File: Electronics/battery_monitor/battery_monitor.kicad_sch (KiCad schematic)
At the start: 23 parts, among them IC1 MIC2779H-1YM5_TR, J2 Conn_01x02_Pin, J2 Conn_01x04_Male, J3 Conn_01x02_Pin, Q2 DMP4015SK3-13, Q4 BSS123LT1G, U1 MCP1700x-120xxMB, U2 INA226

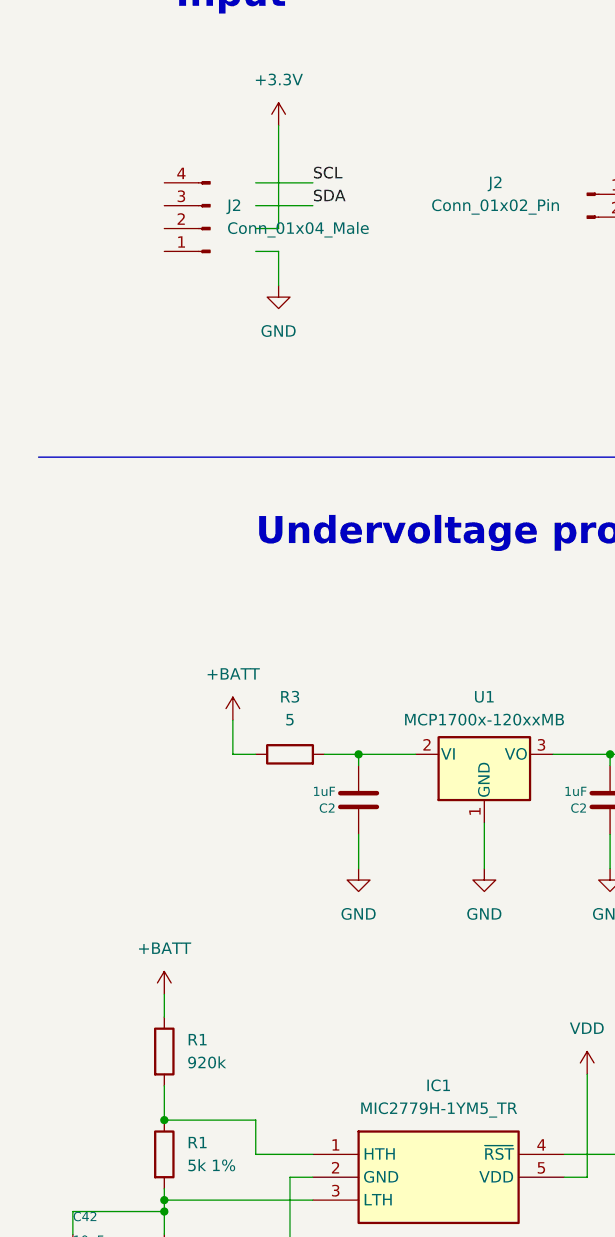
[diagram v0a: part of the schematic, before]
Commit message: Add main robot PCB
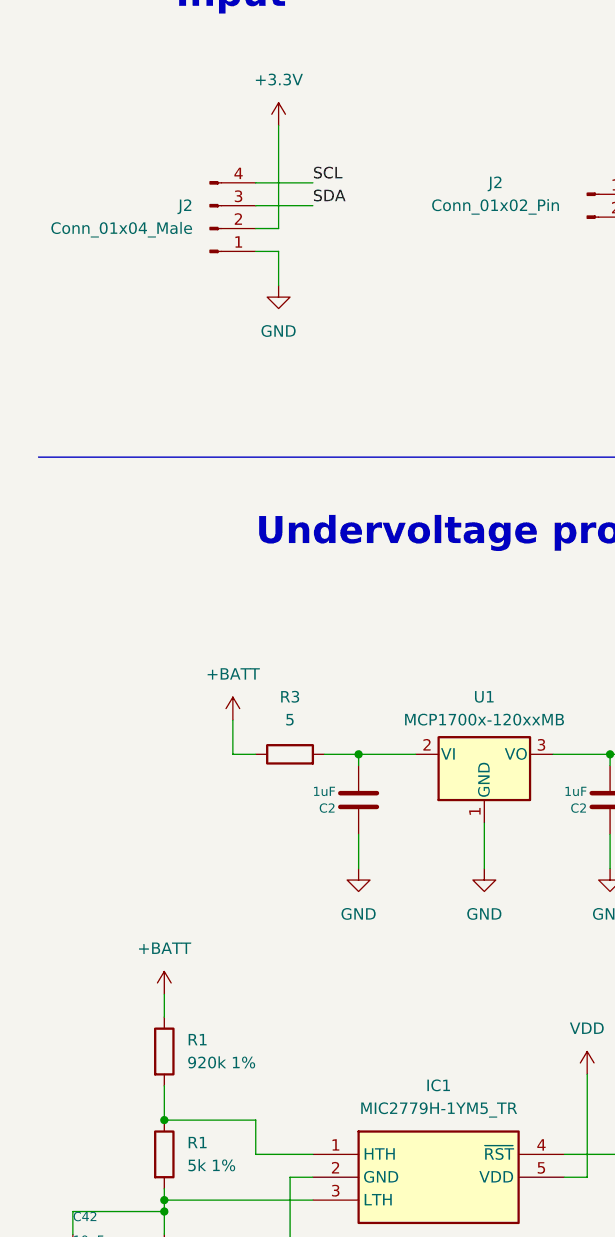
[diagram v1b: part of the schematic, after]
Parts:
- C2: RS (none) -> 103-4095
- JP1, JP2: now left out of the parts list
- R1: Mouser (none) -> 71-CRCW0805-5K
- R1: value 920k -> 920k 1%; Mouser (none) -> 660-RN73H2ATD9203B25
- R1: Mouser (none) -> 603-RC0805FR-0775KL
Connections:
- net +3.3V: now also J2.2 (Pin_2)
- net GND: now also J2.1 (Pin_1)
- net SCL: now also J2.4 (Pin_4)
- net SDA: now also J2.3 (Pin_3)
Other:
- moved on the sheet: J2
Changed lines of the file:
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@@
+      (effects (font (size 1.27 1.27)) hide)
+    )
+    (property "Mouser" " 71-CRCW0805-5K " (at 29.21 149.86 0)
       (effects (font (size 1.27 1.27)) hide)
     )
@@
   (symbol (lib_id "Device:R") (at 29.21 138.43 0) (unit 1)
     (in_bom yes) (on_board yes) (dnp no) (fields_autoplaced)
-    (property "Reference" "R1" (at 31.75 137.1599 0)
-      (effects (font (size 1.27 1.27)) (justify left))
-    )
-    (property "Value" "920k" (at 31.75 139.6999 0)
+    (property "Reference" "R1" (at 31.75 137.16 0)
+      (effects (font (size 1.27 1.27)) (justify left))
+    )
+    (property "Value" "920k 1%" (at 31.75 139.7 0)
       (effects (font (size 1.27 1.27)) (justify left))
     )
@@
     )
     (property "RS" "" (at 29.21 138.43 0)
+      (effects (font (size 1.27 1.27)) hide)
+    )
+    (property "Mouser" " 660-RN73H2ATD9203B25 " (at 29.21 138.43 0)
+      (effects (font (size 1.27 1.27)) hide)
+    )
+    (property "Field6" "" (at 29.21 138.43 0)
       (effects (font (size 1.27 1.27)) hide)
     )
@@
   )
   (symbol (lib_id "Jumper:SolderJumper_3_Open") (at 245.11 53.34 90) (mirror x) (unit 1)
-    (in_bom yes) (on_board yes) (dnp no) (fields_autoplaced)
+    (in_bom no) (on_board yes) (dnp no) (fields_autoplaced)
     (property "Reference" "JP1" (at 242.57 52.07 90)
       (effects (font (size 1.27 1.27)) (justify left))
@@
       (effects (font (size 1.27 1.27)) (justify left bottom) hide)
     )
+    (property "RS" "    103-4095" (at 78.74 110.49 0)
+      (effects (font (size 1.27 1.27)) hide)
+    )
     (pin "1")
     (pin "2")
@@
       (effects (font (size 1.27 1.27)) hide)
     )
-    (property "RS" "" (at 29.21 162.56 0)
+    (property "Mouser" " 603-RC0805FR-0775KL " (at 29.21 162.56 0)
+      (effects (font (size 1.27 1.27)) hide)
+    )
+    (property "Field6" "" (at 29.21 162.56 0)
       (effects (font (size 1.27 1.27)) hide)
     )
@@
     )
   )
-  (symbol (lib_id "Connector:Conn_01x04_Male") (at 34.29 46.99 180) (unit 1)
+  (symbol (lib_id "Connector:Conn_01x04_Male") (at 34.29 46.99 0) (mirror x) (unit 1)
     (in_bom yes) (on_board yes) (dnp no)
-    (property "Reference" "J2" (at 36.195 44.4499 0)
+    (property "Reference" "J2" (at 32.385 44.4499 0)
       (effects (font (size 1.27 1.27)) (justify right))
     )
-    (property "Value" "Conn_01x04_Male" (at 36.195 46.9899 0)
+    (property "Value" "Conn_01x04_Male" (at 32.385 46.9899 0)
       (effects (font (size 1.27 1.27)) (justify right))
     )
@@
   )
   (symbol (lib_id "Jumper:SolderJumper_3_Open") (at 266.7 53.34 270) (unit 1)
-    (in_bom yes) (on_board yes) (dnp no) (fields_autoplaced)
+    (in_bom no) (on_board yes) (dnp no) (fields_autoplaced)
     (property "Reference" "JP2" (at 269.24 52.07 90)
       (effects (font (size 1.27 1.27)) (justify left))
@@
       (effects (font (size 1.27 1.27)) (justify left bottom) hide)
     )
-    (pin "1")
+    (property "RS" "    103-4095" (at 50.8 110.49 0)
+      (effects (font (size 1.27 1.27)) hide)
+    )
+    (pin "1")

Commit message: Main robot PCB order
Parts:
- Q4: value BSS123LT1G -> BS170; RS 545-0135 -> 739-0357
- R1: Mouser 71-CRCW0805-5K -> (none); Mouser Part Number (none) -> 71-CRCW0805-5K
- R1: Mouser 660-RN73H2ATD9203B25 -> (none); Mouser Part Number (none) -> 660-RN73H2ATD9203B25
- R1: Mouser 603-RC0805FR-0775KL -> (none); Mouser Part Number (none) -> 603-RC0805FR-0775KL
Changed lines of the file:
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@@
       (effects (font (size 1.27 1.27)) hide)
     )
-    (property "Mouser" " 71-CRCW0805-5K " (at 29.21 149.86 0)
+    (property "Mouser Part Number" " 71-CRCW0805-5K " (at 29.21 149.86 0)
       (effects (font (size 1.27 1.27)) hide)
     )
@@
       (effects (font (size 1.27 1.27)) hide)
     )
-    (property "Mouser" " 660-RN73H2ATD9203B25 " (at 29.21 138.43 0)
+    (property "Mouser Part Number" " 660-RN73H2ATD9203B25 " (at 29.21 138.43 0)
       (effects (font (size 1.27 1.27)) hide)
     )
@@
       (effects (font (size 1.27 1.27)) (justify left))
     )
-    (property "Value" "BSS123LT1G" (at 92.71 151.13 0)
+    (property "Value" "BS170" (at 92.71 151.13 0)
       (effects (font (size 1.27 1.27)) (justify left))
     )
@@
       (effects (font (size 1.27 1.27)) hide)
     )
-    (property "RS" "    545-0135" (at 86.36 149.86 0)
+    (property "RS" "    739-0357" (at 86.36 149.86 0)
       (effects (font (size 1.27 1.27)) hide)
     )
@@
       (effects (font (size 1.27 1.27)) hide)
     )
-    (property "Mouser" " 603-RC0805FR-0775KL " (at 29.21 162.56 0)
-      (effects (font (size 1.27 1.27)) hide)
-    )
+    (property "Mouser Part Number" " 603-RC0805FR-0775KL " (at 29.21 162.56 0)
+      (effects (font (size 1.27 1.27)) hide)
+    )

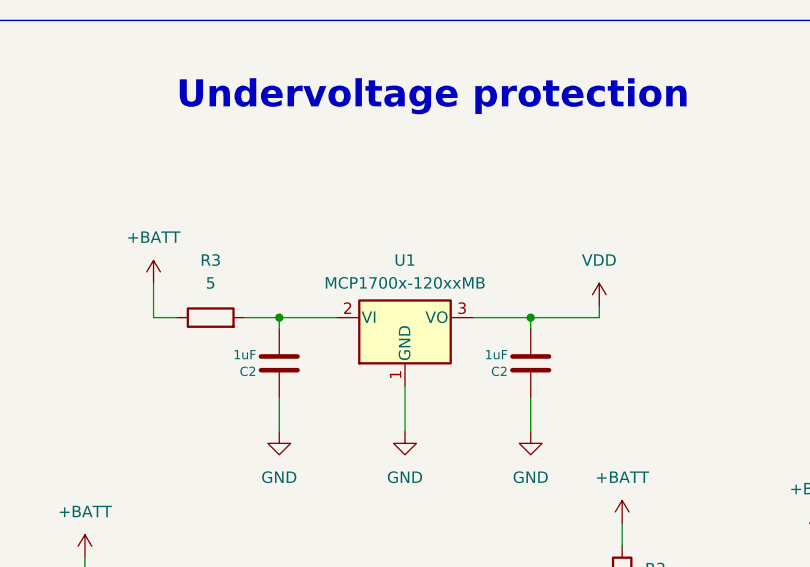
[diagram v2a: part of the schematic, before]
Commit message: Implement fully action-based strategy framework for 2024 robot.
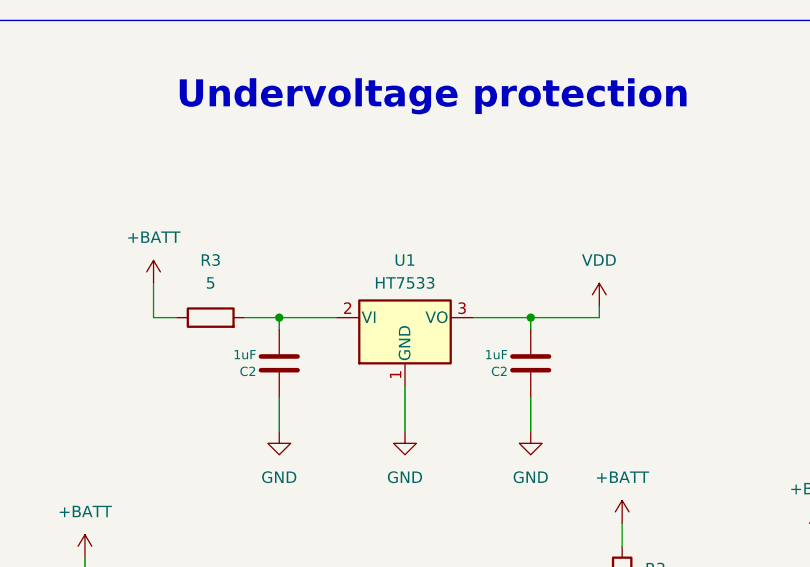
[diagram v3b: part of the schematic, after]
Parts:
- U1: value MCP1700x-120xxMB -> HT7533; RS 669-4923 -> 885-0721
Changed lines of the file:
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@@
       (effects (font (size 1.27 1.27)))
     )
-    (property "Value" "MCP1700x-120xxMB" (at 64.77 101.6 0)
+    (property "Value" "HT7533" (at 64.77 101.6 0)
       (effects (font (size 1.27 1.27)))
     )
@@
       (effects (font (size 1.27 1.27)) hide)
     )
-    (property "RS" "    669-4923" (at 64.77 105.41 0)
+    (property "RS" "    885-0721" (at 64.77 105.41 0)
       (effects (font (size 1.27 1.27)) hide)
     )

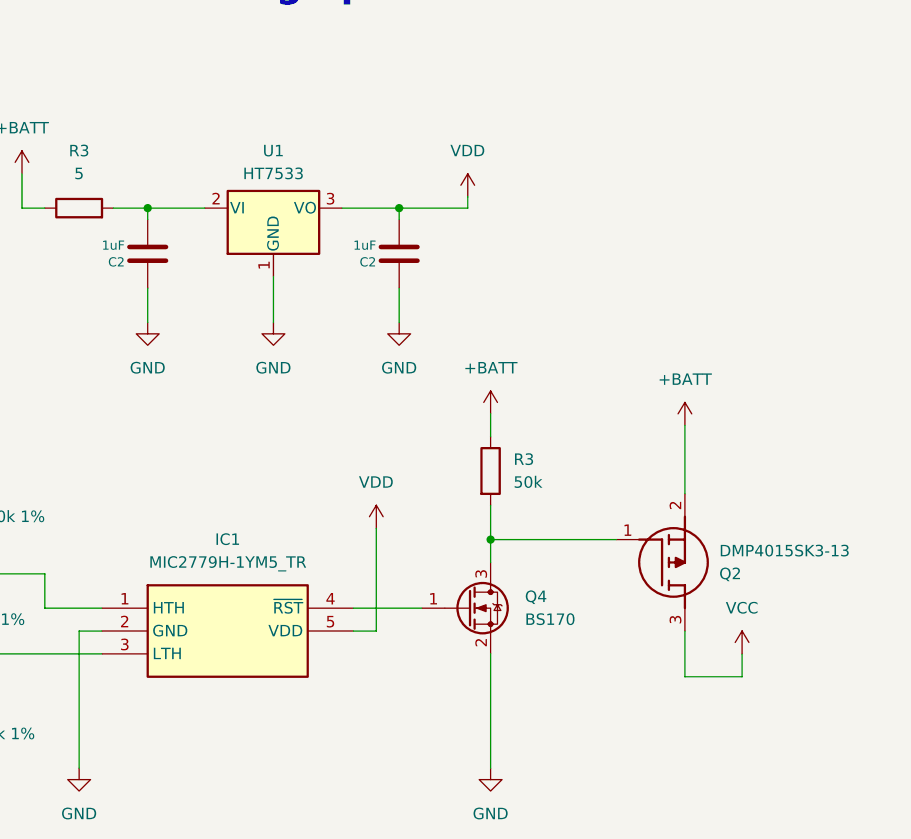
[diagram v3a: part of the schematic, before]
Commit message: Add missing GameState file
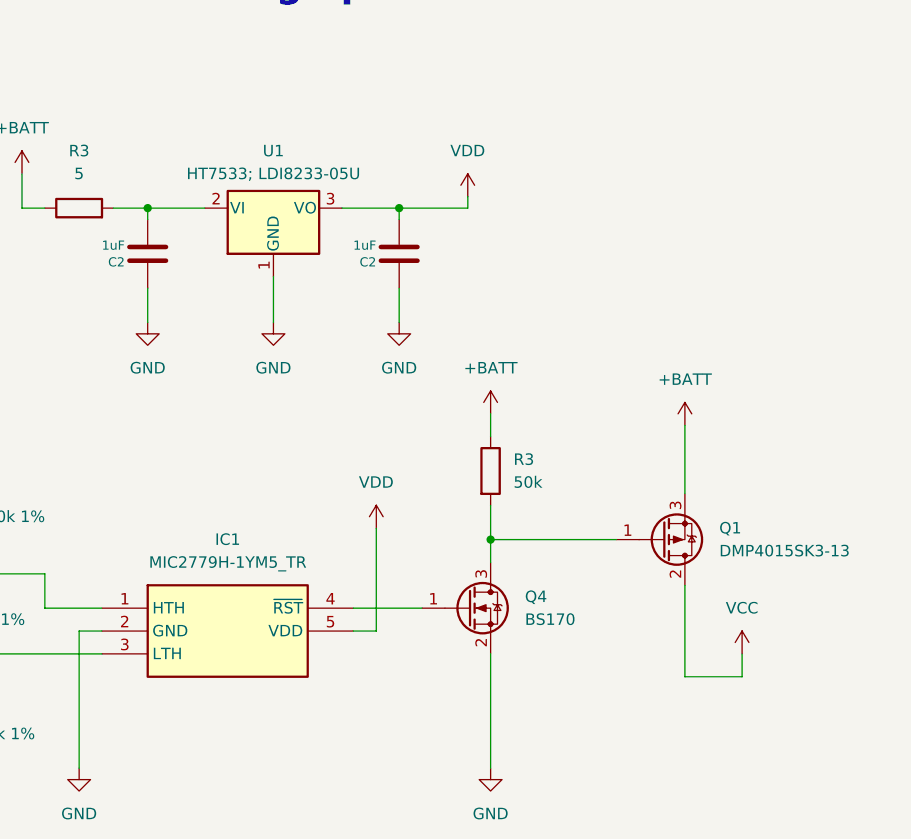
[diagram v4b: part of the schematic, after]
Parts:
- removed Q2: DMP4015SK3-13, MIC2779L-1YM5_TR:AZ1084CD50TRG1, symbol MIC2779L-1YM5_TR:DMP4015SK3-13
- added Q1: DMP4015SK3-13, MIC2779L-1YM5_TR:AZ1084CD50TRG1, symbol Device:Q_PMOS_GDS
- U1: value HT7533 -> HT7533; LDI8233-05U
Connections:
- net +BATT: now also Q1.3 (S)
- net VCC: now also Q1.2 (D)
- net at Q4.3 (D), R3.2: now also Q1.1 (G)
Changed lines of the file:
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@@
     (stroke (width 0) (type default))
   )
-  (wire (pts (xy 110.49 157.48) (xy 110.49 152.4))
+  (wire (pts (xy 110.49 147.32) (xy 110.49 157.48))
     (stroke (width 0) (type default))
   )
@@
       (effects (font (size 1.27 1.27)))
     )
-    (property "Value" "HT7533" (at 64.77 101.6 0)
+    (property "Value" "HT7533; LDI8233-05U" (at 64.77 101.6 0)
       (effects (font (size 1.27 1.27)))
     )
@@
     )
   )
+  (symbol (lib_id "Device:Q_PMOS_GDS") (at 107.95 142.24 0) (mirror x) (unit 1)
+    (in_bom yes) (on_board yes) (dnp no) (fields_autoplaced)
+    (property "Reference" "Q1" (at 114.3 140.97 0)
+      (effects (font (size 1.27 1.27)) (justify left))
+    )
+    (property "Value" "DMP4015SK3-13" (at 114.3 143.51 0)
+      (effects (font (size 1.27 1.27)) (justify left))
+    )
+    (property "Footprint" "MIC2779L-1YM5_TR:AZ1084CD50TRG1" (at 113.03 144.78 0)
+      (effects (font (size 1.27 1.27)) hide)
+    )
+    (property "Datasheet" "~" (at 107.95 142.24 0)
+      (effects (font (size 1.27 1.27)) hide)
+    )
+    (property "Mouser Part Number" "621-DMP4015SK3-13" (at 107.95 142.24 0)
+      (effects (font (size 1.27 1.27)) hide)
+    )
+    (pin "1")
+    (pin "2")
+    (pin "3")
+    (instances
+      (project "battery_monitor"
+        (path "/d060da57-dd7d-4403-be03-0a0a7778ac52"
+          (reference "Q1") (unit 1)
+        )
+      )
+    )
+  )
   (symbol (lib_id "Connector:Conn_01x02_Pin") (at 76.2 43.18 0) (unit 1)
     (in_bom yes) (on_board yes) (dnp no)
@@
         )
       )
-    )
-  )
-  (symbol (lib_id "MIC2779L-1YM5_TR:DMP4015SK3-13") (at 102.87 142.24 0) (mirror x) (unit 1)
-    (in_bom yes) (on_board yes) (dnp no)
-    (property "Reference" "Q2" (at 114.3 146.05 0)
-      (effects (font (size 1.27 1.27)) (justify left))
-    )
-    (property "Value" "DMP4015SK3-13" (at 114.3 143.51 0)
-      (effects (font (size 1.27 1.27)) (justify left))
-    )
-    (property "Footprint" "MIC2779L-1YM5_TR:AZ1084CD50TRG1" (at 114.3 43.51 0)
-      (effects (font (size 1.27 1.27)) (justify left top) hide)
-    )
-    (property "Datasheet" "https://www.diodes.com/assets/Datasheets/DMP4015SK3.pdf" (at 114.3 -56.49 0)
-      (effects (font (size 1.27 1.27)) (justify left top) hide)
-    )
-    (property "Height" "2.38" (at 114.3 -256.49 0)
-      (effects (font (size 1.27 1.27)) (justify left top) hide)
-    )
-    (property "Manufacturer_Name" "Diodes Inc." (at 114.3 -356.49 0)
-      (effects (font (size 1.27 1.27)) (justify left top) hide)
-    )
-    (property "Manufacturer_Part_Number" "DMP4015SK3-13" (at 114.3 -456.49 0)
-      (effects (font (size 1.27 1.27)) (justify left top) hide)
-    )
-    (property "Mouser Part Number" "621-DMP4015SK3-13" (at 114.3 -556.49 0)
-      (effects (font (size 1.27 1.27)) (justify left top) hide)
-    )
-    (property "Mouser Price/Stock" "https://www.mouser.co.uk/ProductDetail/Diodes-Incorporated/DMP4015SK3-13?qs=T%2FOtf55vL7fON%252BtWokt2Lw%3D%3D" (at 114.3 -656.49 0)
-      (effects (font (size 1.27 1.27)) (justify left top) hide)
-    )
-    (property "Arrow Part Number" "DMP4015SK3-13" (at 114.3 -756.49 0)
-      (effects (font (size 1.27 1.27)) (justify left top) hide)
-    )
-    (property "Arrow Price/Stock" "https://www.arrow.com/en/products/dmp4015sk3-13/diodes-incorporated" (at 114.3 -856.49 0)
-      (effects (font (size 1.27 1.27)) (justify left top) hide)
-    )
-    (pin "1")
-    (pin "2")
-    (pin "3")
-    (instances
-      (project "battery_monitor"
-        (path "/d060da57-dd7d-4403-be03-0a0a7778ac52"
-          (reference "Q2") (unit 1)
-        )
-      )
